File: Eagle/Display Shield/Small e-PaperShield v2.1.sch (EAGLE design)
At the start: 115 parts, among them J2 3300060P1-ST-TF-003A, J3 2.54-8p-male-SMD, J4 2.54-8p-male-SMD, J5 2.54-6p-male-SMD, J6 2.54-6p-male-SMD, J7 2.54-2x3p-female-SMD, Q10 MOSFET-P-044021001, Q11 2N7002, Q2 2N7002, Q3 MOSFET-P-044021001, Q5 MOSFET-P-044021001, Q7 MOSFET-P-044021001, Q8 2N7002, Q9 2N7002, SW1 BUTTON-4P-REINFORCE'TS-1188E', U2 XC6206-3.3-1300260P1, U3 74VHC125PW, U4 74VHC125PW, U5 GT20L16P1Y, U7 EPD 1.44/2.0/2.7 inch, U9 S-8120CNB-DRB-TF-G//200021001, X1 FH12-40S-0.5SH

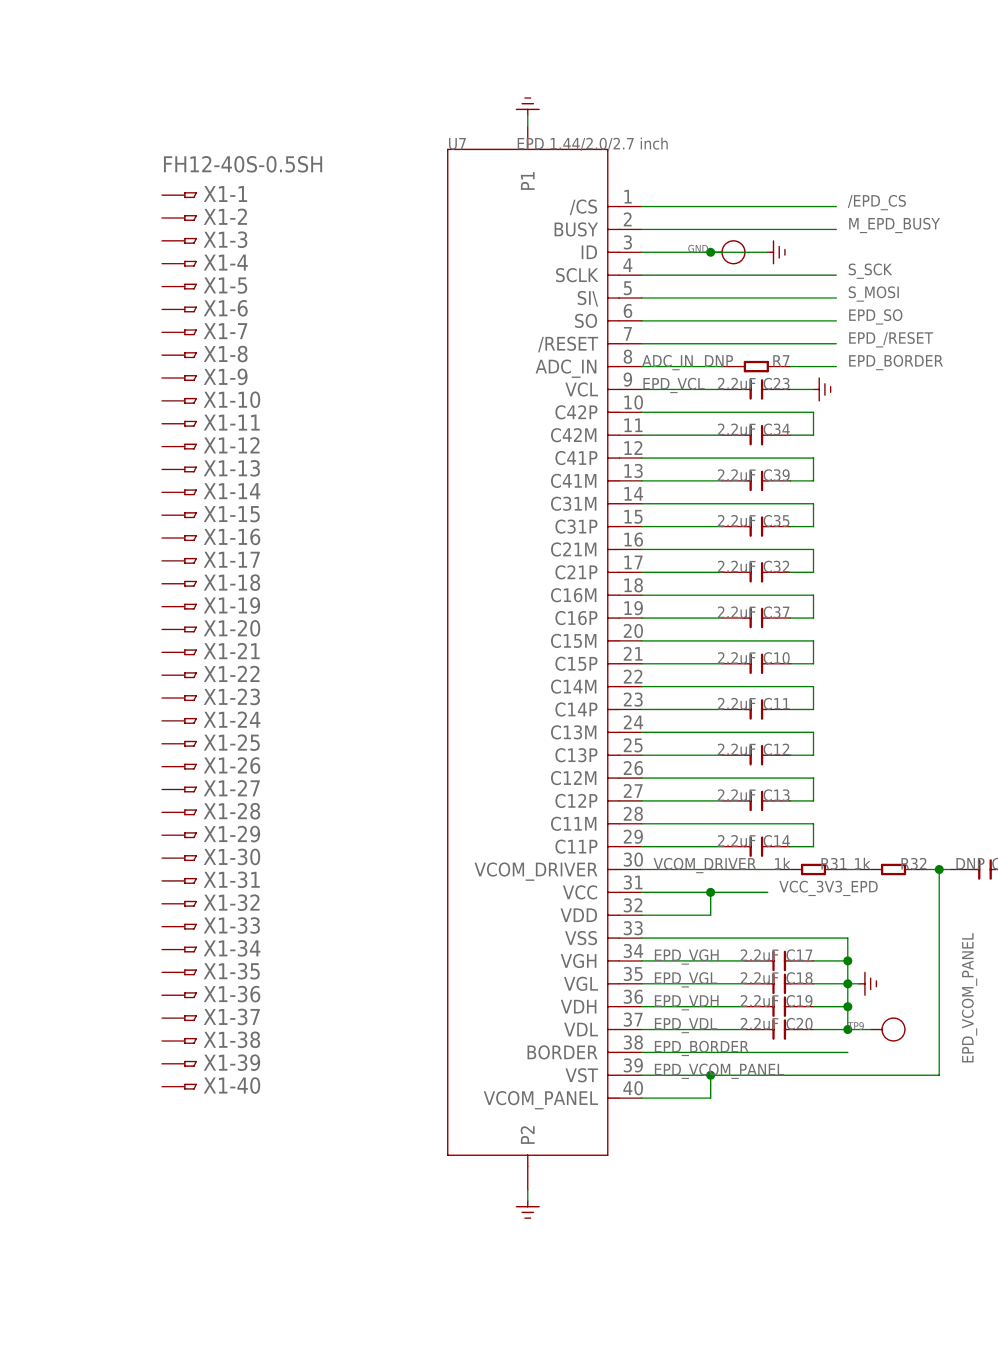
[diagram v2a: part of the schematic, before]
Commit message: reshaped board, snapped components to grid.
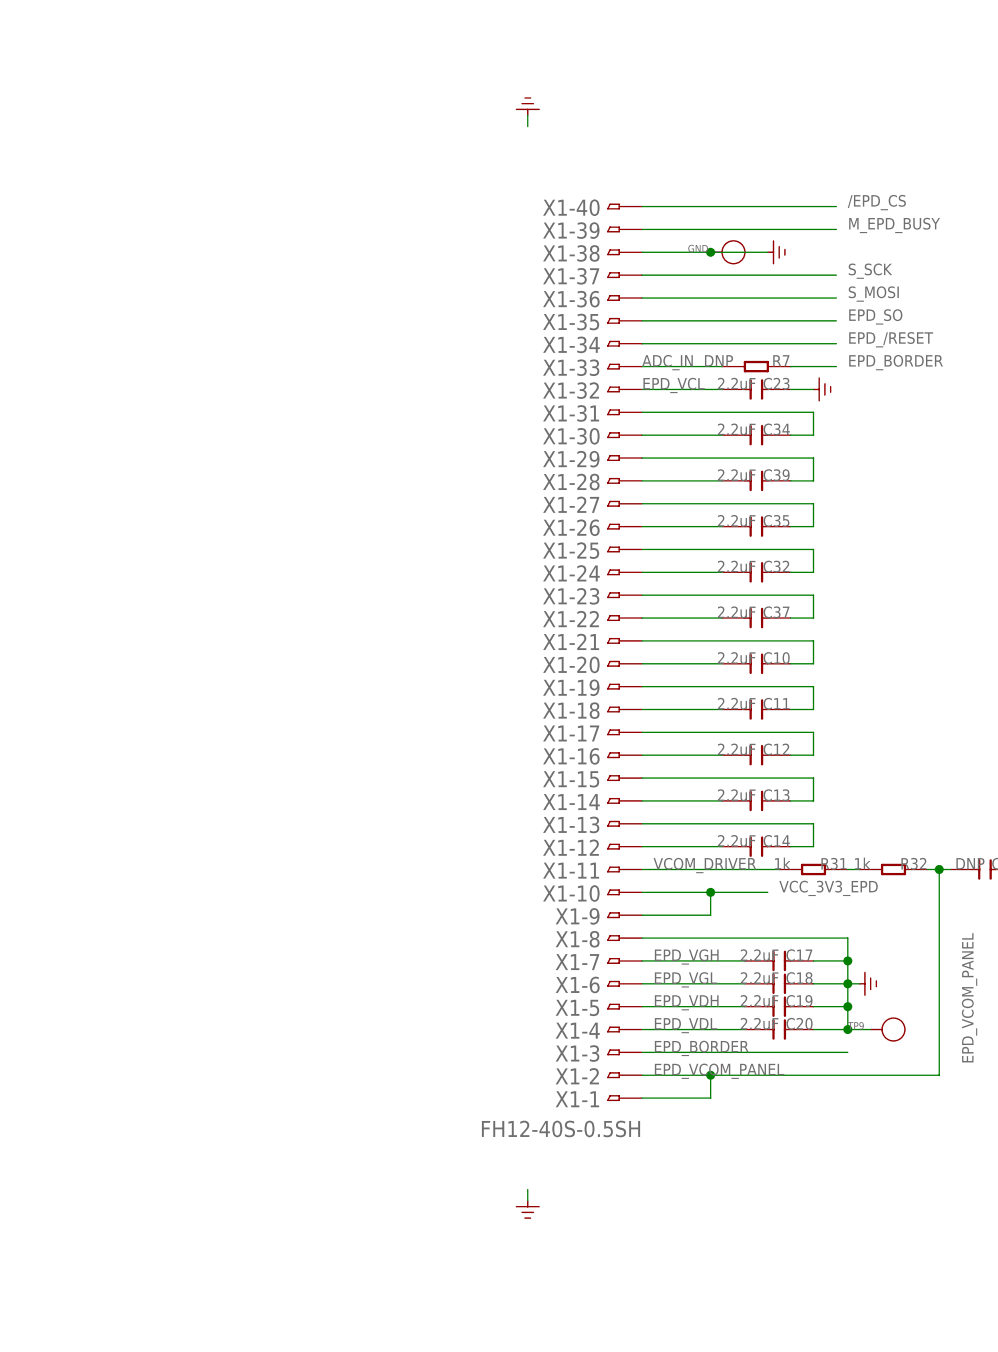
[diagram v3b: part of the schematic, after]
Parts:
- removed U7: EPD 1.44/2.0/2.7 inch, moudle:TFT-EPD-PANEL
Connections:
- net /EPD_CS: now also X1-40.1; no longer U7./CS
- net ADC_IN: now also X1-33.1; no longer U7.ADC_IN
- net EPD_/RESET: now also X1-34.1; no longer U7./RESET
- net EPD_BORDER: now also X1-3.1; no longer U7.BORDER
- net EPD_SO: now also X1-35.1; no longer U7.SO
- net EPD_VCL: now also X1-32.1; no longer U7.VCL
- net EPD_VCOM_PANEL: now also X1-1.1, X1-2.1; no longer U7.VCOM_PANEL, U7.VST
- net EPD_VDH: now also X1-5.1; no longer U7.VDH
- net EPD_VDL: now also X1-4.1; no longer U7.VDL
- net EPD_VGH: now also X1-7.1; no longer U7.VGH
- net EPD_VGL: now also X1-6.1; no longer U7.VGL
- net GND: now also X1-38.1, X1-8.1; no longer U7.ID, U7.P1, U7.P2, U7.VSS
- net M_EPD_BUSY: now also X1-39.1; no longer U7.BUSY
- net N$100: now also X1-13.1; no longer U7.C11M
- net N$101: now also X1-12.1; no longer U7.C11P
- net N$34: now also X1-31.1; no longer U7.C42P
- net N$35: now also X1-30.1; no longer U7.C42M
- net N$36: now also X1-29.1; no longer U7.C41P
- net N$37: now also X1-28.1; no longer U7.C41M
- net N$81: now also X1-27.1; no longer U7.C31M
- net N$85: now also X1-26.1; no longer U7.C31P
- net N$88: now also X1-25.1; no longer U7.C21M
- net N$89: now also X1-24.1; no longer U7.C21P
- net N$90: now also X1-23.1; no longer U7.C16M
- net N$91: now also X1-22.1; no longer U7.C16P
- net N$92: now also X1-21.1; no longer U7.C15M
- net N$93: now also X1-20.1; no longer U7.C15P
- net N$94: now also X1-19.1; no longer U7.C14M
- net N$95: now also X1-18.1; no longer U7.C14P
- net N$96: now also X1-17.1; no longer U7.C13M
- net N$97: now also X1-16.1; no longer U7.C13P
- net N$98: now also X1-15.1; no longer U7.C12M
- net N$99: now also X1-14.1; no longer U7.C12P
- net S_MOSI: now also X1-36.1; no longer U7.SI\
- net S_SCK: now also X1-37.1; no longer U7.SCLK
- net VCC_3V3_EPD: now also X1-10.1, X1-9.1; no longer U7.VCC, U7.VDD
- net VCOM_DRIVER: now also X1-11.1; no longer U7.VCOM_DRIVER
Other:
- moved on the sheet: X1-1, X1-10, X1-11, X1-12, X1-13, X1-14, X1-15, X1-16, X1-17, X1-18, X1-19, X1-2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

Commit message: re-routed most of the traces
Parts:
- removed C52, C53: 100nF, Discrete:C-0603
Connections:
- net GND: no longer C52.1, C53.1
- net VCC_3V3_EPD: no longer C52.2, C53.2
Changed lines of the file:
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@@
 <setting verticaltext="up"/>
 </settings>
-<grid distance="50" unitdist="mil" unit="mil" style="lines" multiple="1" display="no" altdistance="0.01" altunitdist="inch" altunit="inch"/>
+<grid distance="0.1" unitdist="inch" unit="inch" style="lines" multiple="1" display="no" altdistance="0.01" altunitdist="inch" altunit="inch"/>
 <layers>
-<layer number="1" name="Top" color="4" fill="1" visible="yes" active="no"/>
-<layer number="2" name="Route2" color="1" fill="3" visible="yes" active="no"/>
-<layer number="3" name="Route3" color="4" fill="3" visible="yes" active="no"/>
-<layer number="4" name="Route4" color="1" fill="4" visible="yes" active="no"/>
-<layer number="5" name="Route5" color="4" fill="4" visible="yes" active="no"/>
-<layer number="6" name="Route6" color="1" fill="8" visible="yes" active="no"/>
-<layer number="7" name="Route7" color="4" fill="8" visible="yes" active="no"/>
-<layer number="8" name="Route8" color="1" fill="2" visible="yes" active="no"/>
-<layer number="9" name="Route9" color="4" fill="2" visible="yes" active="no"/>
-<layer number="10" name="Route10" color="1" fill="7" visible="yes" active="no"/>
-<layer number="11" name="Route11" color="4" fill="7" visible="yes" active="no"/>
-<layer number="12" name="Route12" color="1" fill="5" visible="yes" active="no"/>
-<layer number="13" name="Route13" color="4" fill="5" visible="yes" active="no"/>
-<layer number="14" name="Route14" color="1" fill="6" visible="yes" active="no"/>
-<layer number="15" name="Route15" color="4" fill="6" visible="yes" active="no"/>
-<layer number="16" name="Bottom" color="1" fill="1" visible="yes" active="no"/>
-<layer number="17" name="Pads" color="2" fill="1" visible="yes" active="no"/>
-<layer number="18" name="Vias" color="2" fill="1" visible="yes" active="no"/>
-<layer number="19" name="Unrouted" color="6" fill="1" visible="yes" active="no"/>
-<layer number="20" name="Dimension" color="5" fill="1" visible="yes" active="no"/>
-<layer number="21" name="tPlace" color="7" fill="1" visible="yes" active="no"/>
-<layer number="22" name="bPlace" color="3" fill="1" visible="yes" active="no"/>
-<layer number="23" name="tOrigins" color="15" fill="1" visible="yes" active="no"/>
-<layer number="24" name="bOrigins" color="3" fill="1" visible="yes" active="no"/>
-<layer number="25" name="tNames" color="7" fill="1" visible="yes" active="no"/>
-<layer number="26" name="bNames" color="3" fill="1" visible="yes" active="no"/>
-<layer number="27" name="tValues" color="7" fill="1" visible="yes" active="no"/>
-<layer number="28" name="bValues" color="7" fill="1" visible="yes" active="no"/>
+<layer number="1" name="Top" color="4" fill="1" visible="no" active="no"/>
+<layer number="2" name="Route2" color="1" fill="3" visible="no" active="no"/>
+<layer number="3" name="Route3" color="4" fill="3" visible="no" active="no"/>
+<layer number="4" name="Route4" color="1" fill="4" visible="no" active="no"/>
+<layer number="5" name="Route5" color="4" fill="4" visible="no" active="no"/>
+<layer number="6" name="Route6" color="1" fill="8" visible="no" active="no"/>
+<layer number="7" name="Route7" color="4" fill="8" visible="no" active="no"/>
+<layer number="8" name="Route8" color="1" fill="2" visible="no" active="no"/>
+<layer number="9" name="Route9" color="4" fill="2" visible="no" active="no"/>
+<layer number="10" name="Route10" color="1" fill="7" visible="no" active="no"/>
+<layer number="11" name="Route11" color="4" fill="7" visible="no" active="no"/>
+<layer number="12" name="Route12" color="1" fill="5" visible="no" active="no"/>
+<layer number="13" name="Route13" color="4" fill="5" visible="no" active="no"/>
+<layer number="14" name="Route14" color="1" fill="6" visible="no" active="no"/>
+<layer number="15" name="Route15" color="4" fill="6" visible="no" active="no"/>
+<layer number="16" name="Bottom" color="1" fill="1" visible="no" active="no"/>
+<layer number="17" name="Pads" color="2" fill="1" visible="no" active="no"/>
+<layer number="18" name="Vias" color="2" fill="1" visible="no" active="no"/>
+<layer number="19" name="Unrouted" color="6" fill="1" visible="no" active="no"/>
+<layer number="20" name="Dimension" color="5" fill="1" visible="no" active="no"/>
+<layer number="21" name="tPlace" color="7" fill="1" visible="no" active="no"/>
+<layer number="22" name="bPlace" color="3" fill="1" visible="no" active="no"/>
+<layer number="23" name="tOrigins" color="15" fill="1" visible="no" active="no"/>
+<layer number="24" name="bOrigins" color="3" fill="1" visible="no" active="no"/>
+<layer number="25" name="tNames" color="7" fill="1" visible="no" active="no"/>
+<layer number="26" name="bNames" color="3" fill="1" visible="no" active="no"/>
+<layer number="27" name="tValues" color="7" fill="1" visible="no" active="no"/>
+<layer number="28" name="bValues" color="7" fill="1" visible="no" active="no"/>
 <layer number="29" name="tStop" color="7" fill="3" visible="no" active="no"/>
 <layer number="30" name="bStop" color="3" fill="6" visible="no" active="no"/>
@@
 <layer number="35" name="tGlue" color="7" fill="4" visible="no" active="no"/>
 <layer number="36" name="bGlue" color="3" fill="5" visible="no" active="no"/>
-<layer number="37" name="tTest" color="7" fill="1" visible="yes" active="no"/>
-<layer number="38" name="bTest" color="3" fill="1" visible="yes" active="no"/>
+<layer number="37" name="tTest" color="7" fill="1" visible="no" active="no"/>
+<layer number="38" name="bTest" color="3" fill="1" visible="no" active="no"/>
 <layer number="39" name="tKeepout" color="4" fill="11" visible="no" active="no"/>
 <layer number="40" name="bKeepout" color="1" fill="11" visible="no" active="no"/>
@@
 <layer number="44" name="Drills" color="7" fill="1" visible="no" active="no"/>
 <layer number="45" name="Holes" color="7" fill="1" visible="no" active="no"/>
-<layer number="46" name="Milling" color="3" fill="1" visible="yes" active="no"/>
-<layer number="47" name="Measures" color="7" fill="1" visible="yes" active="no"/>
-<layer number="48" name="Document" color="7" fill="1" visible="yes" active="no"/>
-<layer number="49" name="Reference" color="7" fill="1" visible="yes" active="no"/>
-<layer number="50" name="dxf" color="7" fill="1" visible="yes" active="no"/>
-<layer number="51" name="tDocu" color="7" fill="1" visible="yes" active="no"/>
-<layer number="52" name="bDocu" color="7" fill="1" visible="yes" active="no"/>
-<layer number="53" name="tGND_GNDA" color="7" fill="9" visible="yes" active="no"/>
-<layer number="54" name="bGND_GNDA" color="1" fill="9" visible="yes" active="no"/>
-<layer number="56" name="wert" color="7" fill="1" visible="yes" active="no"/>
+<layer number="46" name="Milling" color="3" fill="1" visible="no" active="no"/>
+<layer number="47" name="Measures" color="7" fill="1" visible="no" active="no"/>
+<layer number="48" name="Document" color="7" fill="1" visible="no" active="no"/>
+<layer number="49" name="Reference" color="7" fill="1" visible="no" active="no"/>
+<layer number="50" name="dxf" color="7" fill="1" visible="no" active="no"/>
+<layer number="51" name="tDocu" color="7" fill="1" visible="no" active="no"/>
+<layer number="52" name="bDocu" color="7" fill="1" visible="no" active="no"/>
+<layer number="53" name="tGND_GNDA" color="7" fill="9" visible="no" active="no"/>
+<layer number="54" name="bGND_GNDA" color="1" fill="9" visible="no" active="no"/>
+<layer number="56" name="wert" color="7" fill="1" visible="no" active="no"/>
 <layer number="91" name="Nets" color="2" fill="1" visible="yes" active="yes"/>
 <layer number="92" name="Busses" color="1" fill="1" visible="yes" active="yes"/>
@@
 <part name="R20" library="Discrete" deviceset="R-4R*" device="-1206" value="100k"/>
 <part name="R16" library="Discrete" deviceset="R-4R*" device="-1206" value="100k"/>
-<part name="C52" library="Discrete" deviceset="C*" device="-0603" value="100nF"/>
-<part name="C53" library="Discrete" deviceset="C*" device="-0603" value="100nF"/>
 <part name="T_VGL" library="Discrete" deviceset="PAD-TEST-POINT" device="'3535'"/>
 <part name="T_VGH" library="Discrete" deviceset="PAD-TEST-POINT" device="'3535'"/>
@@
 <instance part="R16" gate="C" x="-31.75" y="54.61" rot="R180"/>
 <instance part="R16" gate="D" x="-31.75" y="49.53" rot="R180"/>
-<instance part="C52" gate="C" x="-217.17" y="16.51" rot="R90"/>
-<instance part="C53" gate="C" x="-214.63" y="16.51" rot="R90"/>
 <instance part="T_VGL" gate="TP" x="-111.76" y="116.84" rot="R90"/>
 <instance part="T_VGH" gate="TP" x="-35.56" y="166.37" rot="R90"/>
@@
 <wire x1="-240.03" y1="8.89" x2="-240.03" y2="6.35" width="0.1524" layer="91"/>
 <pinref part="U$4" gate="G$1" pin="GND"/>
-<pinref part="C53" gate="C" pin="1"/>
-<wire x1="-214.63" y1="12.7" x2="-214.63" y2="8.89" width="0.1524" layer="91"/>
-<wire x1="-214.63" y1="8.89" x2="-217.17" y2="8.89" width="0.1524" layer="91"/>
-<junction x="-219.71" y="8.89"/>
-<pinref part="C52" gate="C" pin="1"/>
-<wire x1="-217.17" y1="8.89" x2="-219.71" y2="8.89" width="0.1524" layer="91"/>
-<wire x1="-217.17" y1="12.7" x2="-217.17" y2="8.89" width="0.1524" layer="91"/>
-<junction x="-217.17" y="8.89"/>
 </segment>
 <segment>
@@
 <wire x1="-222.25" y1="26.67" x2="-219.71" y2="26.67" width="0.1524" layer="91"/>
 <label x="-224.79" y="33.02" size="1.27" layer="95" ratio="10"/>
-<pinref part="C52" gate="C" pin="2"/>
-<wire x1="-219.71" y1="26.67" x2="-217.17" y2="26.67" width="0.1524" layer="91"/>
-<wire x1="-217.17" y1="26.67" x2="-217.17" y2="20.32" width="0.1524" layer="91"/>
 <junction x="-219.71" y="26.67"/>
-<pinref part="C53" gate="C" pin="2"/>
-<wire x1="-217.17" y1="26.67" x2="-214.63" y2="26.67" width="0.1524" layer="91"/>
-<wire x1="-214.63" y1="26.67" x2="-214.63" y2="20.32" width="0.1524" layer="91"/>
-<junction x="-217.17" y="26.67"/>
 <wire x1="-219.71" y1="26.67" x2="-219.71" y2="31.75" width="0.1524" layer="91"/>
 <junction x="-219.71" y="26.67"/>

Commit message: DRC corrections for display shield
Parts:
- removed PWR: led-green, Discrete:LED'RIGHT'
- removed R5: 1k, Discrete:R-0603
- removed RST: led-red, Discrete:LED'RIGHT'
- removed SW1: BUTTON-4P-REINFORCE'TS-1188E', Discrete:BUTTON-4P-REINFORCE'TS-1188E'
- added LED0: LED0, adafruit:LEDCHIPLED_0603
- added LED1: LED1, adafruit:LEDCHIPLED_0603
- added R1: 1k, rcl:R-EU_R0603
- R2: device Discrete:R-0603 -> rcl:R-EU_R0603
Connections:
- removed net M_CKV: J5.3
- removed net M_OE123: J5.2
- removed net M_RESET: J6.6, RST.-, SW1.2
- removed net M_STV_IN: J5.4
- removed net N$87: R5.2, RST.+
- new net BTN0: J5.2, S8.3, S8.4
- new net BTN1: J5.3, S7.3, S7.4
- new net BTN2: J5.4, S6.3, S6.4
- new net BTN3: J5.5, S5.3, S5.4
- new net LED0: J3.2, R1.2
- new net LED1: J3.1, R2.2
- new net N$17: LED1.A, R2.1
- net GND: now also LED0.C, LED1.C, S5.1, S5.2, S6.1, S6.2, S7.1, S7.2, S8.1, S8.2; no longer R2.2, SW1.1, SW1.S1, SW1.S2
- net N$1: now also LED0.A, R1.1; no longer PWR.-, R2.1
- net VCC_3V3: no longer PWR.+, R5.1
